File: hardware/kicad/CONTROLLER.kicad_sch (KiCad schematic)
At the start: 0 parts

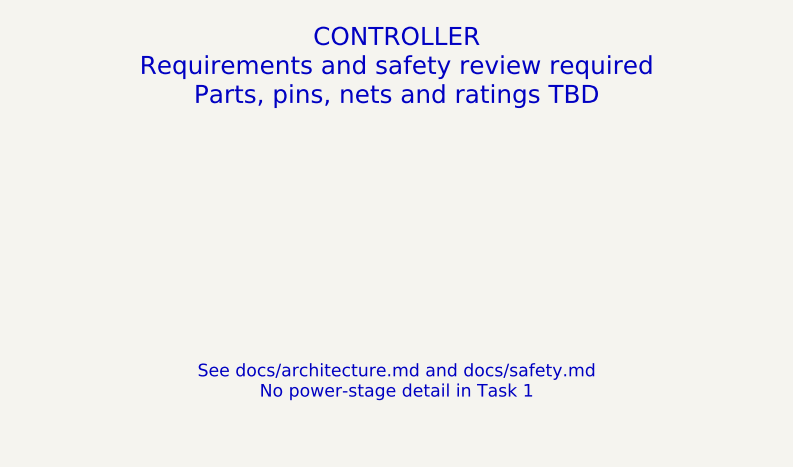
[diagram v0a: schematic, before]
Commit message: hardware: update existing KiCad architecture and add precharge sheet
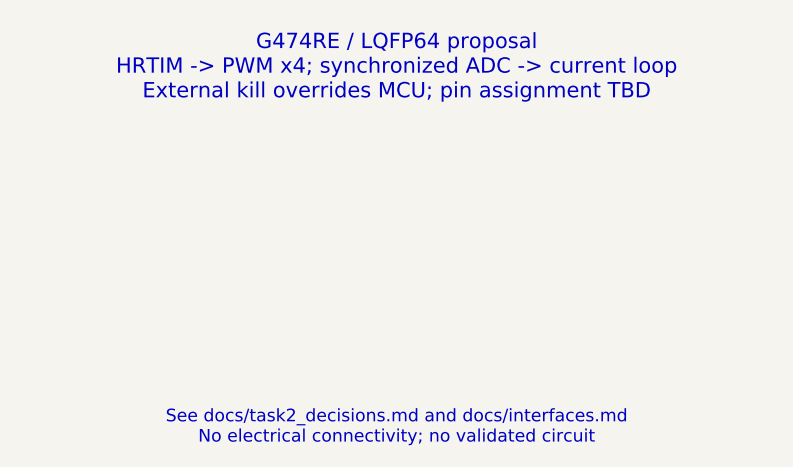
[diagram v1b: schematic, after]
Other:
- note added: "G474RE / LQFP64 proposal HRTIM -> PWM x4; synchronized ADC -> current loop External kill overrides MCU; pin assignment TBD"
- note added: "See docs/task2_decisions.md and docs/interfaces.md No electrical connectivity; no validated circuit"
- note removed: "CONTROLLER Requirements and safety review required Parts, pins, nets and ratings TBD"
- note removed: "See docs/architecture.md and docs/safety.md No power-stage detail in Task 1"
- title: CONTROLLER - Placeholder -> CONTROLLER - Task 2 Proposal

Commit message: hardware: implement prototype Rev A electrical schematic
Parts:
- added C30, C31, C32, C33, C36, C38: 100nF / 16V X7R, Capacitor_SMD:C_0805_2012Metric, symbol RevA:C
- added C34: 4.7uF /16V X7R, Capacitor_SMD:C_0805_2012Metric, symbol RevA:C
- added C35, C37: 1uF /16V, Capacitor_SMD:C_0805_2012Metric, symbol RevA:C
- added C39: 100nF, Capacitor_SMD:C_0805_2012Metric, symbol RevA:C
- added J10: 3.3V UART / no power pin, Connector_PinHeader_2.54mm:PinHeader_1x03_P2.54mm_Vertical, symbol RevA:J3
- added J9: SWD reference voltage ONLY / do not externally po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, Connector_PinHeader_2.54mm:PinHeader_1x06_P2.54mm_Vertical, symbol RevA:J6
- added R75: 10R, Resistor_SMD:R_0805_2012Metric, symbol RevA:R
- added R76: 0R, Resistor_SMD:R_0805_2012Metric, symbol RevA:R
- added R77, R78, R79, R80, R81, R82, R83, R84, R85, R86, R87: 10k, Resistor_SMD:R_0805_2012Metric, symbol RevA:R
- added U7: STM32G474RET6, Package_QFP:LQFP-64_10x10mm_P0.5mm, symbol RevA:STM32G474RET6
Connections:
- new net ARM_PULSE: R83.1 (A), U7.24 (PB0)
- new net BUS_ISO_FB: U7.57 (PB4)
- new net BUS_ISO_REQUEST: U7.38 (PC6)
- new net BUS_I_ADC: U7.18 (PA4)
- new net BUS_RAW_ADC: U7.11 (PC3)
- new net BUS_V_ADC: U7.12 (PA0)
- new net BYP_BUS_FB: U7.59 (PB6)
- new net BYP_BUS_REQUEST: U7.33 (PB11)
- new net BYP_CAP_FB: U7.60 (PB7)
- new net BYP_CAP_REQUEST: U7.41 (PC9)
- new net CAN_RX: R78.1 (A), U7.61 (PB8)
- new net CAN_STANDBY: U7.54 (PC12)
- new net CAN_TX: U7.62 (PB9)
- new net CAP_ISO_FB: U7.58 (PB5)
- new net CAP_ISO_REQUEST: U7.39 (PC7)
- new net CAP_I_ADC: U7.19 (PA5)
- new net CAP_RAW_ADC: U7.22 (PC4)
- new net CAP_V_ADC: U7.13 (PA1)
- new net DUMP_REQUEST: U7.52 (PC10)
- new net GND: C30.2 (B), C31.2 (B), C32.2 (B), C33.2 (B), C34.2 (B), C35.2 (B), C36.2 (B), C37.2 (B), C38.2 (B), C39.2 (B), J10.3 (P3), J9.6 (P6), R79.2 (B), R80.2 (B), R81.2 (B), R82.2 (B), R83.2 (B), R84.2 (B), R85.2 (B), R86.2 (B), U7.15 (VSS), U7.27 (VSSA), U7.31 (VSS), U7.47 (VSS), U7.63 (VSS)
- new net HW_FAULT_N: U7.46 (PA12)
- new net IL_I_ADC: U7.20 (PA6)
- new net MCU_GATE_REQUEST: R84.1 (A), U7.26 (PB2)
- new net MON_ALERT_HOST: U7.53 (PC11)
- new net MON_CONFIG_VALID: R86.1 (A), U7.55 (PD2)
- new net MON_CS_HOST: R87.1 (A), U7.34 (PB12)
- new net MON_MISO_HOST: U7.36 (PB14)
- new net MON_MOSI_HOST: U7.37 (PB15)
- new net MON_SCLK_HOST: U7.35 (PB13)
- new net NRST: C39.1 (A), J9.5 (P5), R77.1 (A), U7.7 (PG10)
- new net PRE_BUS_FB: U7.51 (PA15)
- new net PRE_BUS_REQUEST: U7.30 (PB10)
- new net PRE_CAP_FB: U7.2 (PC13)
- new net PRE_CAP_REQUEST: U7.40 (PC8)
- new net PWM_AH: R79.1 (A), U7.42 (PA8)
- new net PWM_AL: R80.1 (A), U7.43 (PA9)
- new net PWM_BH: R81.1 (A), U7.44 (PA10)
- new net PWM_BL: R82.1 (A), U7.45 (PA11)
- new net REFEREE_PERMIT: U7.23 (PC5)
- new net SWCLK: J9.3 (P3), U7.50 (PA14)
- new net SWDIO: J9.2 (P2), U7.49 (PA13)
- new net SWO: J9.4 (P4), U7.56 (PB3)
- new net TEMP_BANK_ADC: U7.10 (PC2)
- new net TEMP_FET_ADC: U7.8 (PC0)
- new net TEMP_L_ADC: U7.9 (PC1)
- new net UART_RX: J10.2 (P2), U7.17 (PA3)
- new net UART_TX: J10.1 (P1), U7.14 (PA2)
- new net V3V3: C30.1 (A), C31.1 (A), C32.1 (A), C33.1 (A), C34.1 (A), J9.1 (P1), R75.1 (A), R77.2 (B), R78.2 (B), R87.2 (B), U7.1 (VBAT), U7.16 (VDD), U7.32 (VDD), U7.48 (VDD), U7.64 (VDD)
- new net VDDA: C35.1 (A), C36.1 (A), R75.2 (B), R76.1 (A), U7.29 (VDDA)
- new net VREF_ADC: C37.1 (A), C38.1 (A), R76.2 (B), U7.28 (VREF+)
- new net WD_HEARTBEAT: R85.1 (A), U7.25 (PB1)
- no-connect marks 0 -> 5
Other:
- note added: "ADC HRTIM-synchronized sampling; internal comparators are secondary diagnostics, not primary OC shutdown."
- note added: "HSI clock for draft, no external crystal. FDCAN bit timing/HSI accuracy must be checked before robot integration."
- note added: "PG10 pin7 configured NRST; PB8 pin61 BOOT0 strap/options: boot configuration must be locked to flash before use."
- note removed: "G474RE / LQFP64 proposal HRTIM -> PWM x4; synchronized ADC -> current loop External kill overrides MCU; pin assignment TBD"
- note removed: "See docs/task2_decisions.md and docs/interfaces.md No electrical connectivity; no validated circuit"
- title: CONTROLLER - Task 2 Proposal -> CONTROLLER / Prototype Rev A draft

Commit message: hardware: refine Rev A protection and passive selections
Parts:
- removed C30, C31, C32, C33, C36, C38: 100nF / 16V X7R, Capacitor_SMD:C_0805_2012Metric, symbol RevA:C
- removed C34: 4.7uF /16V X7R, Capacitor_SMD:C_0805_2012Metric, symbol RevA:C
- removed C35, C37: 1uF /16V, Capacitor_SMD:C_0805_2012Metric, symbol RevA:C
- removed C39: 100nF, Capacitor_SMD:C_0805_2012Metric, symbol RevA:C
- removed J10: 3.3V UART / no power pin, Connector_PinHeader_2.54mm:PinHeader_1x03_P2.54mm_Vertical, symbol RevA:J3
- removed J9: SWD reference voltage ONLY / do not externally po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, Connector_PinHeader_2.54mm:PinHeader_1x06_P2.54mm_Vertical, symbol RevA:J6
- removed R82, R83, R84, R85, R86, R87: 10k, Resistor_SMD:R_0805_2012Metric, symbol RevA:R
- removed U7: STM32G474RET6, Package_QFP:LQFP-64_10x10mm_P0.5mm, symbol RevA:STM32G474RET6
- added C40, C41, C42, C43, C46, C48: 100nF / 16V X7R, Capacitor_SMD:C_0805_2012Metric, symbol RevA:C
- added C44: 4.7uF /16V X7R, Capacitor_SMD:C_0805_2012Metric, symbol RevA:C
- added C45, C47: 1uF /16V, Capacitor_SMD:C_0805_2012Metric, symbol RevA:C
- added C49: 100nF, Capacitor_SMD:C_0805_2012Metric, symbol RevA:C
- added J6: SWD reference voltage ONLY / do not externally po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, Connector_PinHeader_2.54mm:PinHeader_1x06_P2.54mm_Vertical, symbol RevA:J6
- added J7: 3.3V UART / no power pin, Connector_PinHeader_2.54mm:PinHeader_1x03_P2.54mm_Vertical, symbol RevA:J3
- added R69: 10R, Resistor_SMD:R_0805_2012Metric, symbol RevA:R
- added R70: 0R, Resistor_SMD:R_0805_2012Metric, symbol RevA:R
- added R71, R72, R73, R74: 10k, Resistor_SMD:R_0805_2012Metric, symbol RevA:R
- added U11: STM32G474RET6, Package_QFP:LQFP-64_10x10mm_P0.5mm, symbol RevA:STM32G474RET6
- R75: value 10R -> 10k; MPN (none) -> CRCW080510K0FKEA
- R76: value 0R -> 10k; MPN (none) -> CRCW080510K0FKEA
- R77, R78, R79, R80, R81: MPN (none) -> CRCW080510K0FKEA
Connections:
- net ARM_PULSE: now also R77.1 (A), U11.24 (PB0)
- net BUS_ISO_FB: now also U11.57 (PB4)
- net BUS_ISO_REQUEST: now also U11.38 (PC6)
- net BUS_I_ADC: now also U11.18 (PA4)
- net BUS_RAW_ADC: now also U11.11 (PC3)
- net BUS_V_ADC: now also U11.12 (PA0)
- net BYP_BUS_FB: now also U11.59 (PB6)
- net BYP_BUS_REQUEST: now also U11.33 (PB11)
- net BYP_CAP_FB: now also U11.60 (PB7)
- net BYP_CAP_REQUEST: now also U11.41 (PC9)
- net CAN_RX: now also R72.1 (A), U11.61 (PB8); no longer R78.1 (A)
- net CAN_STANDBY: now also U11.54 (PC12)
- net CAN_TX: now also U11.62 (PB9)
- net CAP_ISO_FB: now also U11.58 (PB5)
- net CAP_ISO_REQUEST: now also U11.39 (PC7)
- net CAP_I_ADC: now also U11.19 (PA5)
- net CAP_RAW_ADC: now also U11.22 (PC4)
- net CAP_V_ADC: now also U11.13 (PA1)
- net DUMP_REQUEST: now also U11.52 (PC10)
- net GND: now also R75.2 (B), R76.2 (B), R77.2 (B), R78.2 (B), C40.2 (B), C41.2 (B), C42.2 (B), C43.2 (B), C44.2 (B), C45.2 (B), C46.2 (B), C47.2 (B), C48.2 (B), C49.2 (B), J6.6 (P6), J7.3 (P3), R73.2 (B), R74.2 (B), U11.15 (VSS), U11.27 (VSSA), U11.31 (VSS), U11.47 (VSS), U11.63 (VSS); no longer R81.2 (B)
- net HW_FAULT_N: now also U11.46 (PA12)
- net IL_I_ADC: now also U11.20 (PA6)
- net MCU_GATE_REQUEST: now also R78.1 (A), U11.26 (PB2)
- net MON_ALERT_HOST: now also U11.53 (PC11)
- net MON_CONFIG_VALID: now also R80.1 (A), U11.55 (PD2)
- net MON_CS_HOST: now also R81.1 (A), U11.34 (PB12)
- net MON_MISO_HOST: now also U11.36 (PB14)
- net MON_MOSI_HOST: now also U11.37 (PB15)
- net MON_SCLK_HOST: now also U11.35 (PB13)
- net NRST: now also C49.1 (A), J6.5 (P5), R71.1 (A), U11.7 (PG10); no longer R77.1 (A)
- net PRE_BUS_FB: now also U11.51 (PA15)
- net PRE_BUS_REQUEST: now also U11.30 (PB10)
- net PRE_CAP_FB: now also U11.2 (PC13)
- net PRE_CAP_REQUEST: now also U11.40 (PC8)
- net PWM_AH: now also R73.1 (A), U11.42 (PA8); no longer R79.1 (A)
- net PWM_AL: now also R74.1 (A), U11.43 (PA9); no longer R80.1 (A)
- net PWM_BH: now also R75.1 (A), U11.44 (PA10); no longer R81.1 (A)
- net PWM_BL: now also R76.1 (A), U11.45 (PA11)
- net REFEREE_PERMIT: now also U11.23 (PC5)
- net SWCLK: now also J6.3 (P3), U11.50 (PA14)
- net SWDIO: now also J6.2 (P2), U11.49 (PA13)
- net SWO: now also J6.4 (P4), U11.56 (PB3)
- net TEMP_BANK_ADC: now also U11.10 (PC2)
- net TEMP_FET_ADC: now also U11.8 (PC0)
- net TEMP_L_ADC: now also U11.9 (PC1)
- net UART_RX: now also J7.2 (P2), U11.17 (PA3)
- net UART_TX: now also J7.1 (P1), U11.14 (PA2)
- net V3V3: now also R81.2 (B), C40.1 (A), C41.1 (A), C42.1 (A), C43.1 (A), C44.1 (A), J6.1 (P1), R69.1 (A), R71.2 (B), R72.2 (B), U11.1 (VBAT), U11.16 (VDD), U11.32 (VDD), U11.48 (VDD), U11.64 (VDD); no longer R75.1 (A), R77.2 (B), R78.2 (B)
- net VDDA: now also C45.1 (A), C46.1 (A), R69.2 (B), R70.1 (A), U11.29 (VDDA); no longer R75.2 (B), R76.1 (A)
- net VREF_ADC: now also C47.1 (A), C48.1 (A), R70.2 (B), U11.28 (VREF+); no longer R76.2 (B)
- net WD_HEARTBEAT: now also R79.1 (A), U11.25 (PB1)
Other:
- moved on the sheet: R75, R76, R77, R78, R79, R80, R81
